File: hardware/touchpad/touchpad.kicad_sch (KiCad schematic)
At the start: 3 parts, among them J1 Conn_01x26_MountingPin, J2 Conn_01x26_MountingPin, J3 Conn_01x26_MountingPin

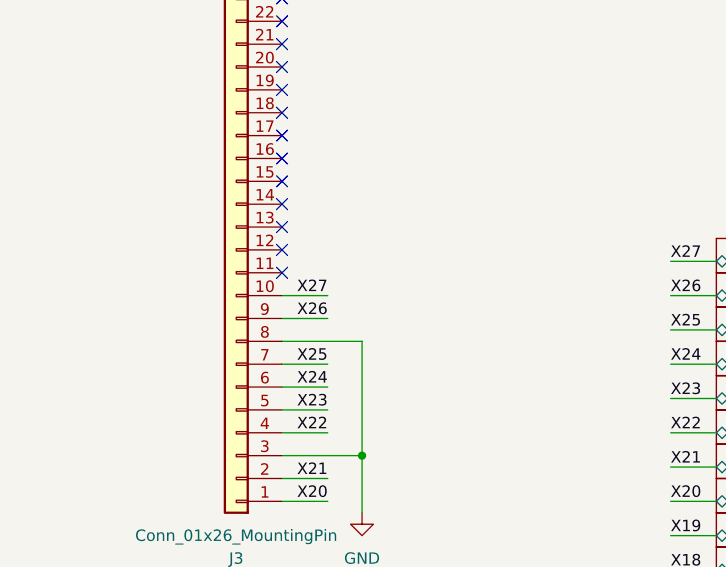
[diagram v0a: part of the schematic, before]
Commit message: finished touchpad
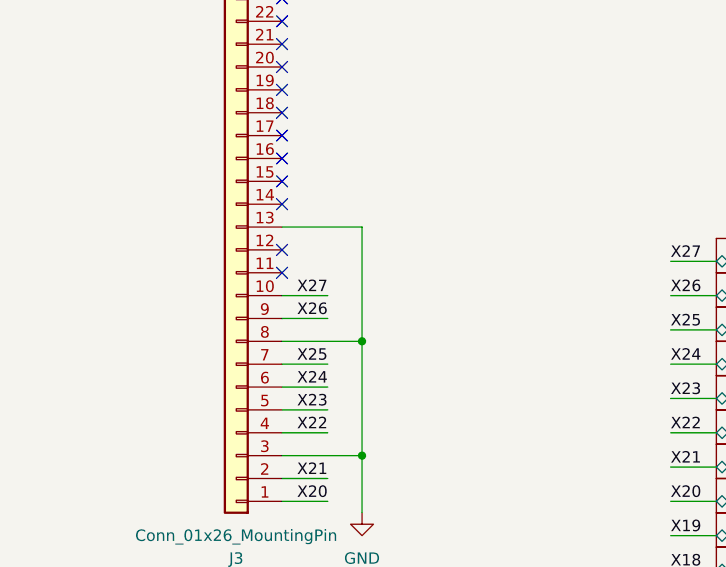
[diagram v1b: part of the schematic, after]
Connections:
- net GND: now also J3.13 (Pin_13)
- no-connect marks 22 -> 21
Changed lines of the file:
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@@
+	)
+	(junction
+		(at 64.77 73.66)
+		(diameter 0)
+		(color 0 0 0 0)
 	)
 	(junction
@@
 	)
 	(no_connect
-		(at 55.88 60.96)
-	)
-	(no_connect
 		(at 55.88 35.56)
 	)
@@
 	(wire
 		(pts
+			(xy 64.77 60.96) (xy 55.88 60.96)
+		)
+		(stroke
+			(width 0)
+			(type default)
+		)
+	)
+	(wire
+		(pts
 			(xy 99.06 99.06) (xy 104.14 99.06)
 		)
@@
 		)
 		(stroke
+			(width 0)
+			(type default)
+		)
+	)
+	(wire
+		(pts
+			(xy 64.77 73.66) (xy 64.77 60.96)
+		)
+		(stroke

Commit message: started schematics
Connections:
- no-connect marks 21 -> 22
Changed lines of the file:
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@@
+	)
+	(no_connect
+		(at 50.8 22.86)
 	)
 	(no_connect

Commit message: fixed stuff
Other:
- title: (none) -> Linea Touchpad
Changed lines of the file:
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@@
 	(generator_version "9.0")
 	(paper "A4")
+	(title_block
+		(title "Linea Touchpad")
+	)
 	(junction
 		(at 224.79 91.44)

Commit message: bunch o f stuff
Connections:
- net GND: now also J1.14 (Pin_14), J1.19 (Pin_19), J1.24 (Pin_24), J1.4 (Pin_4), J1.9 (Pin_9), J2.14 (Pin_14), J2.19 (Pin_19), J2.24 (Pin_24), J2.4 (Pin_4), J2.9 (Pin_9), J3.14 (Pin_14), J3.19 (Pin_19), J3.24 (Pin_24); no longer J1.13 (Pin_13), J1.18 (Pin_18), J1.23 (Pin_23), J1.3 (Pin_3), J1.8 (Pin_8), J2.13 (Pin_13), J2.18 (Pin_18), J2.23 (Pin_23), J2.3 (Pin_3), J2.8 (Pin_8), J3.13 (Pin_13), J3.3 (Pin_3), J3.8 (Pin_8)
- net X0: now also J2.26 (Pin_26); no longer J2.1 (Pin_1)
- net X1: now also J2.25 (Pin_25); no longer J2.2 (Pin_2)
- net X10: now also J2.13 (Pin_13); no longer J2.14 (Pin_14)
- net X11: now also J2.12 (Pin_12); no longer J2.15 (Pin_15)
- net X12: now also J2.11 (Pin_11); no longer J2.16 (Pin_16)
- net X13: now also J2.10 (Pin_10); no longer J2.17 (Pin_17)
- net X14: now also J2.8 (Pin_8); no longer J2.19 (Pin_19)
- net X15: now also J2.7 (Pin_7); no longer J2.20 (Pin_20)
- net X16: now also J2.6 (Pin_6); no longer J2.21 (Pin_21)
- net X17: now also J2.5 (Pin_5); no longer J2.22 (Pin_22)
- net X18: now also J2.3 (Pin_3); no longer J2.24 (Pin_24)
- net X19: now also J2.2 (Pin_2); no longer J2.25 (Pin_25)
- net X2: now also J2.23 (Pin_23); no longer J2.4 (Pin_4)
- net X20: now also J3.26 (Pin_26); no longer J3.1 (Pin_1)
- net X21: now also J3.25 (Pin_25); no longer J3.2 (Pin_2)
- net X22: now also J3.23 (Pin_23); no longer J3.4 (Pin_4)
- net X23: now also J3.22 (Pin_22); no longer J3.5 (Pin_5)
- net X24: now also J3.21 (Pin_21); no longer J3.6 (Pin_6)
- net X25: now also J3.20 (Pin_20); no longer J3.7 (Pin_7)
- net X26: now also J3.18 (Pin_18); no longer J3.9 (Pin_9)
- net X27: now also J3.17 (Pin_17); no longer J3.10 (Pin_10)
- net X3: now also J2.22 (Pin_22); no longer J2.5 (Pin_5)
- net X4: now also J2.21 (Pin_21); no longer J2.6 (Pin_6)
- net X5: now also J2.20 (Pin_20); no longer J2.7 (Pin_7)
- net X6: now also J2.18 (Pin_18); no longer J2.9 (Pin_9)
- net X7: now also J2.17 (Pin_17); no longer J2.10 (Pin_10)
- net X8: now also J2.16 (Pin_16); no longer J2.11 (Pin_11)
- net X9: now also J2.15 (Pin_15); no longer J2.12 (Pin_12)
- net Y0: now also J1.26 (Pin_26); no longer J1.1 (Pin_1)
- net Y1: now also J1.25 (Pin_25); no longer J1.2 (Pin_2)
- net Y10: now also J1.13 (Pin_13); no longer J1.14 (Pin_14)
- net Y11: now also J1.12 (Pin_12); no longer J1.15 (Pin_15)
- net Y12: now also J1.11 (Pin_11); no longer J1.16 (Pin_16)
- net Y13: now also J1.10 (Pin_10); no longer J1.17 (Pin_17)
- net Y14: now also J1.8 (Pin_8); no longer J1.19 (Pin_19)
- net Y15: now also J1.7 (Pin_7); no longer J1.20 (Pin_20)
- net Y16: now also J1.6 (Pin_6); no longer J1.21 (Pin_21)
- net Y17: now also J1.5 (Pin_5); no longer J1.22 (Pin_22)
- net Y2: now also J1.23 (Pin_23); no longer J1.4 (Pin_4)
- net Y3: now also J1.22 (Pin_22); no longer J1.5 (Pin_5)
- net Y4: now also J1.21 (Pin_21); no longer J1.6 (Pin_6)
- net Y5: now also J1.20 (Pin_20); no longer J1.7 (Pin_7)
- net Y6: now also J1.18 (Pin_18); no longer J1.9 (Pin_9)
- net Y7: now also J1.17 (Pin_17); no longer J1.10 (Pin_10)
- net Y8: now also J1.16 (Pin_16); no longer J1.11 (Pin_11)
- net Y9: now also J1.15 (Pin_15); no longer J1.12 (Pin_12)
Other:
- moved on the sheet: J1, J2, J3
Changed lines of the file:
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@@
 	)
 	(no_connect
-		(at 170.18 57.15)
+		(at 50.8 96.52)
 	)
 	(no_connect
@@
 	)
 	(no_connect
-		(at 40.64 110.49)
-	)
-	(no_connect
 		(at 45.72 115.57)
 	)
 	(no_connect
-		(at 50.8 22.86)
-	)
-	(no_connect
 		(at 175.26 64.77)
 	)
@@
 	)
 	(no_connect
+		(at 40.64 184.15)
+	)
+	(no_connect
 		(at 55.88 48.26)
 	)
@@
 	)
 	(no_connect
+		(at 170.18 130.81)
+	)
+	(no_connect
 		(at 55.88 30.48)
 	)
@@
 	(symbol
 		(lib_id "Connector_Generic_MountingPin:Conn_01x26_MountingPin")
-		(at 40.64 148.59 180)
+		(at 40.64 146.05 0)
+		(mirror y)
 		(unit 1)
 		(exclude_from_sim no)
@@
 		(on_board yes)
 		(dnp no)
-		(fields_autoplaced yes)
 		(property "Reference" "J2"
-			(at 40.64 185.42 0)
+			(at 40.64 109.22 0)
 			(effects
 				(font
@@
 		)
 		(property "Value" "Conn_01x26_MountingPin"
-			(at 40.64 182.88 0)
+			(at 40.64 111.76 0)
 			(effects
 				(font
@@
 		)
 		(property "Footprint" "FPC:Hirose_FH12-26S-0.5SH(55)-FPC_1"
-			(at 40.64 148.59 0)
+			(at 40.64 146.05 0)
 			(effects
 				(font
@@
 		)
 		(property "Datasheet" "~"
-			(at 40.64 148.59 0)
+			(at 40.64 146.05 0)
 			(effects
 				(font
@@
 		)
 		(property "Description" "Generic connectable mounting pin connector, single row, 01x26, script generated (kicad-library-utils/schlib/autogen/connector/)"
-			(at 40.64 148.59 0)
+			(at 40.64 146.05 0)
 			(effects
 				(font
@@
 	(symbol
 		(lib_id "Connector_Generic_MountingPin:Conn_01x26_MountingPin")
-		(at 50.8 60.96 180)
+		(at 50.8 58.42 0)
+		(mirror y)
 		(unit 1)
 		(exclude_from_sim no)
@@
 		(dnp no)
 		(property "Reference" "J3"
-			(at 50.8 97.79 0)
+			(at 50.8 21.59 0)
 			(effects
 				(font
@@
 		)
 		(property "Value" "Conn_01x26_MountingPin"
-			(at 50.8 95.25 0)
+			(at 50.8 24.13 0)
 			(effects
 				(font
@@
 		)
 		(property "Footprint" "FPC:Hirose_FH12-26S-0.5SH(55)-FPC_1"
-			(at 50.8 60.96 0)
+			(at 50.8 58.42 0)
 			(effects
 				(font
@@
 		)
 		(property "Datasheet" "~"
-			(at 50.8 60.96 0)
+			(at 50.8 58.42 0)
 			(effects
 				(font
@@
 		)
 		(property "Description" "Generic connectable mounting pin connector, single row, 01x26, script generated (kicad-library-utils/schlib/autogen/connector/)"
-			(at 50.8 60.96 0)
+			(at 50.8 58.42 0)
 			(effects
 				(font
@@
 	(symbol
 		(lib_id "Connector_Generic_MountingPin:Conn_01x26_MountingPin")
-		(at 170.18 95.25 180)
+		(at 170.18 92.71 0)
+		(mirror y)
 		(unit 1)
 		(exclude_from_sim no)
@@
 		(on_board yes)
 		(dnp no)
-		(fields_autoplaced yes)
 		(property "Reference" "J1"
-			(at 170.18 132.08 0)
+			(at 170.18 55.88 0)
 			(effects
 				(font
@@
 		)
 		(property "Value" "Conn_01x26_MountingPin"
-			(at 170.18 129.54 0)
+			(at 170.18 58.42 0)
 			(effects
 				(font
@@
 		)
 		(property "Footprint" "FPC:Hirose_FH12-26S-0.5SH(55)-FPC_1"
-			(at 170.18 95.25 0)
+			(at 170.18 92.71 0)
 			(effects
 				(font
@@
 		)
 		(property "Datasheet" "~"
-			(at 170.18 95.25 0)
+			(at 170.18 92.71 0)
 			(effects
 				(font
@@
 		)
 		(property "Description" "Generic connectable mounting pin connector, single row, 01x26, script generated (kicad-library-utils/schlib/autogen/connector/)"
-			(at 170.18 95.25 0)
+			(at 170.18 92.71 0)
 			(effects
 				(font
